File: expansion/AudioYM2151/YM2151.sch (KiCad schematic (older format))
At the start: 14 parts

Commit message: More work on YM2151
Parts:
- added C? (x5): 100nF, symbol Device:C
- added RN?: R_Network05, Resistor_THT:R_Array_SIP6, symbol Device:R_Network05
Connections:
- net GNDA is gone; now on net GND: C?.1, C?.1, C?.2, C?.2, U?.11 (V-), U?.16 (AGND), U?.8 (AGND)
- net +5V: now also C?.1, C?.1, C?.1, C?.1, C?.1, RN?.1 (common)
- net GND: now also C?.2, C?.2, C?.2, C?.2, C?.2
- net ~IRQ: now also RN?.2 (R1)
- net at U?.19 (SH2), U?.5 (SAM2): now also RN?.5 (R4)
- net at U?.20 (SH1), U?.6 (SAM1): now also RN?.4 (R3)
- net at U?.21 (SO), U?.4 (SD): now also RN?.3 (R2)
- net at U?.2 (CLK1), U?.23 (1): now also RN?.6 (R5)
- net D0 renamed D8
- net D1 renamed D9
- net D2 renamed D10
- net D3 renamed D11
- net D4 renamed D12
- net D5 renamed D13
- net D6 renamed D14
- net D7 renamed D15
- net SPI_YMCLK renamed CS_YMCLK
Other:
- moved on the sheet: C?, R?, U?, U?A, U?B, U?C, U?D, U?E

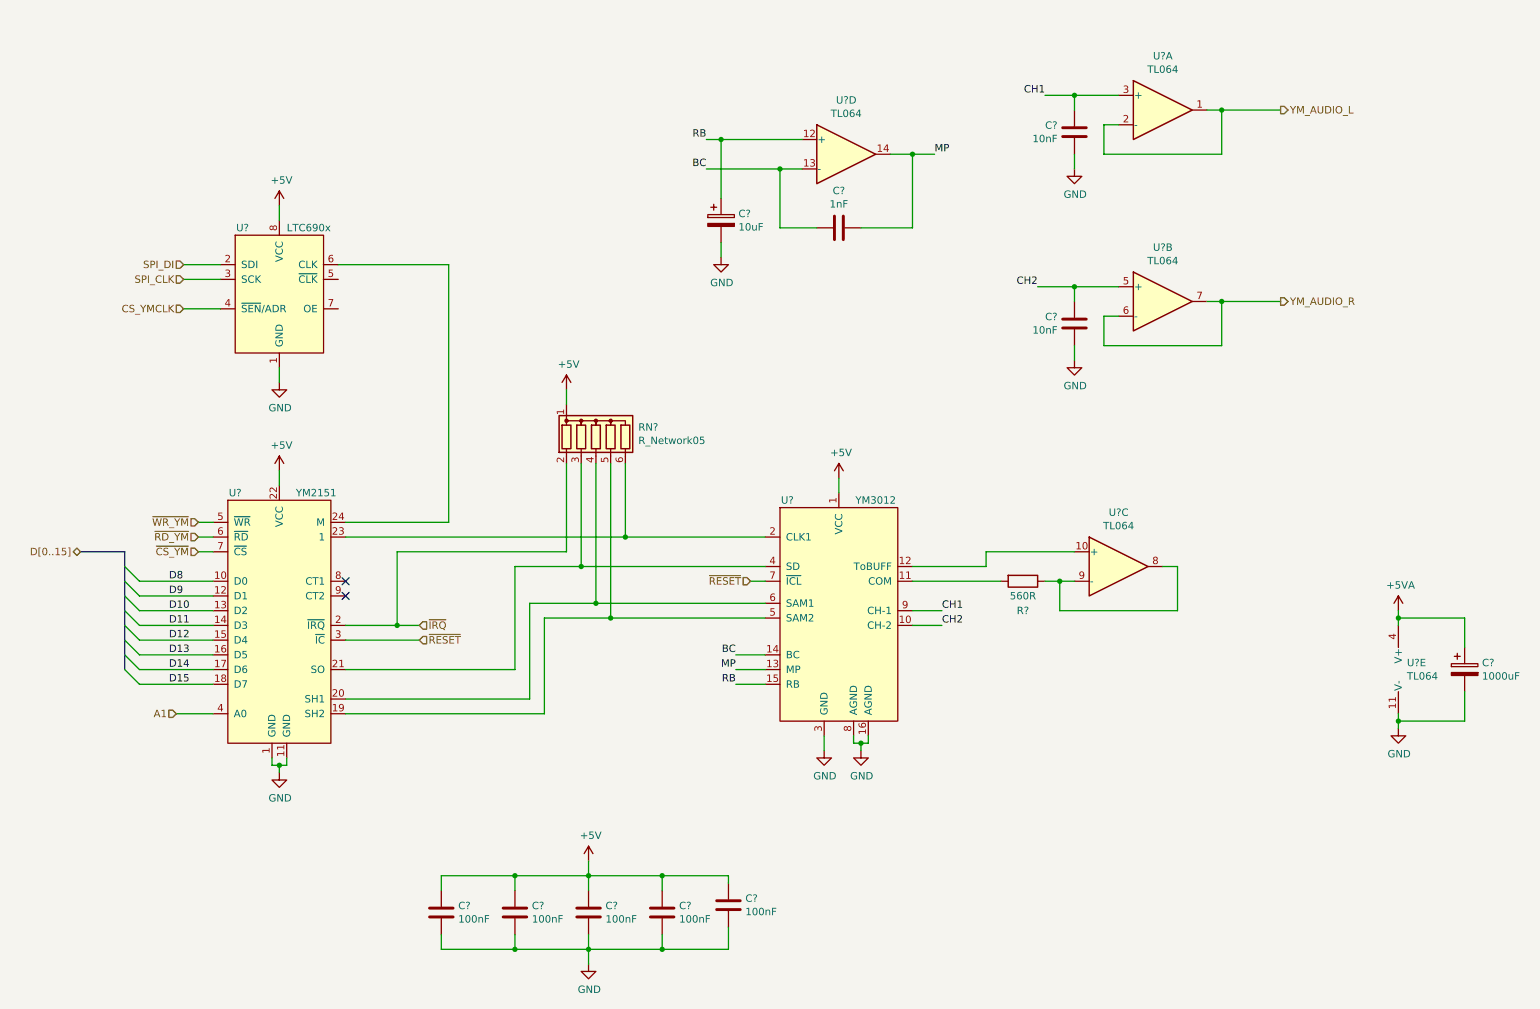
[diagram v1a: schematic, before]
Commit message: Started YM2151 board layout
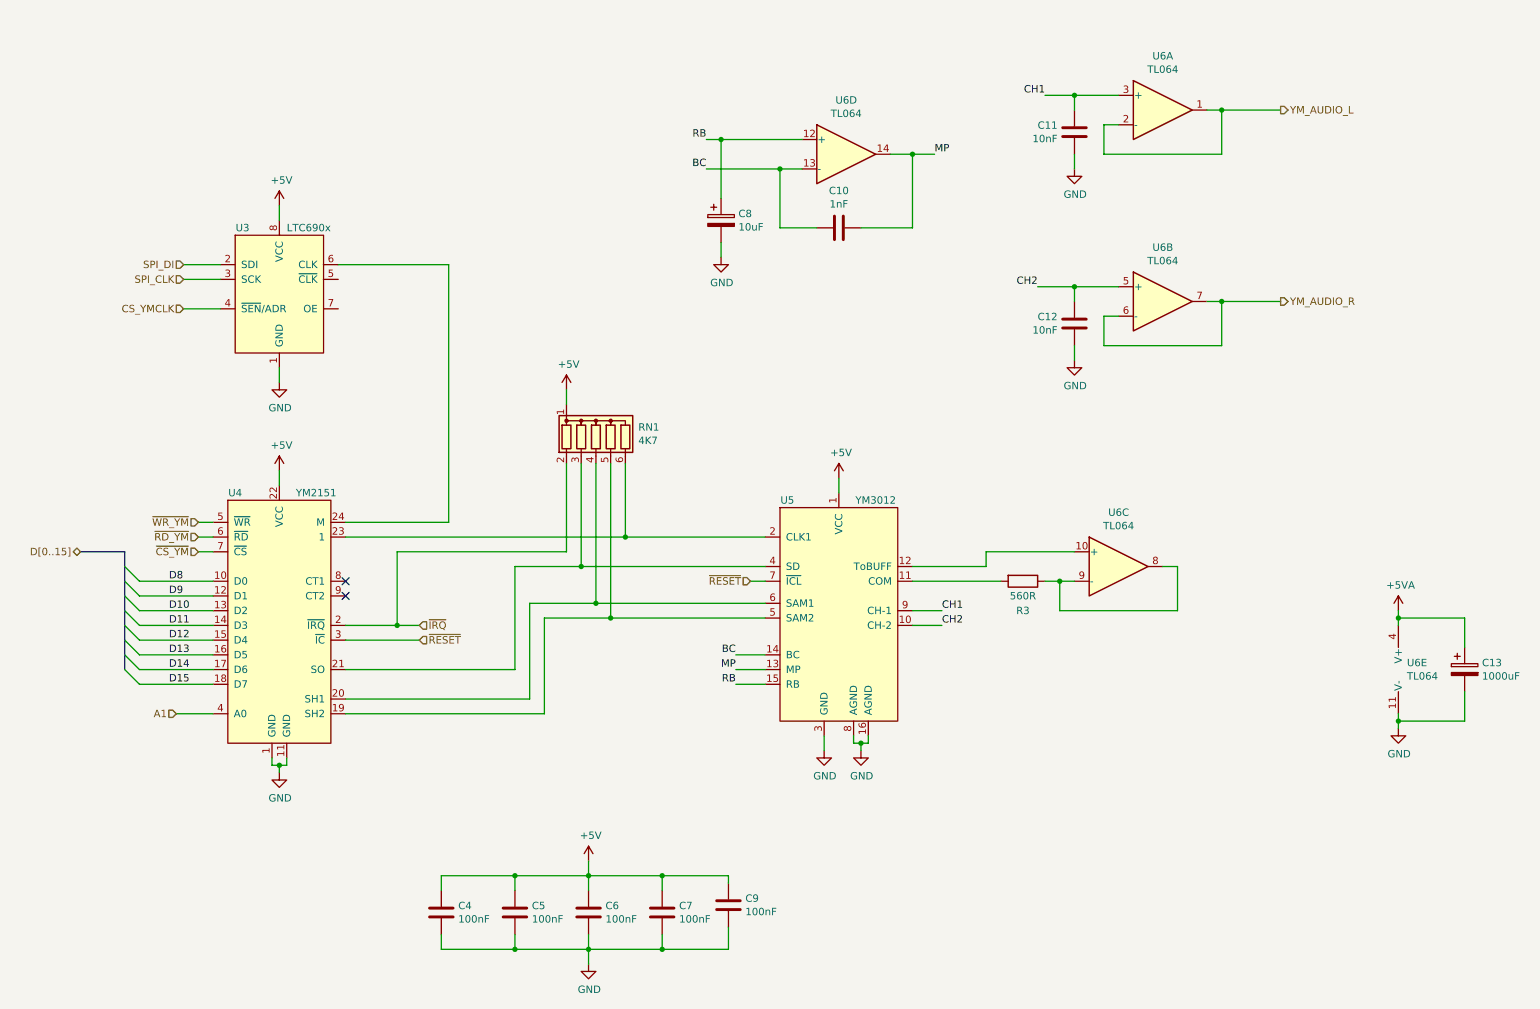
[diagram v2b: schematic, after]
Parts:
- C10, C11, C12, C4, C5, C6, C7, C9: renamed from C?; footprint (none) -> Capacitor_THT:C_Disc_D5.0mm_W2.5mm_P2.50mm
- C13: renamed from C?; footprint (none) -> Capacitor_THT:CP_Radial_D8.0mm_P5.00mm
- C8: renamed from C?; footprint (none) -> Capacitor_THT:CP_Radial_D5.0mm_P2.50mm
- R3: renamed from R?; footprint (none) -> Resistor_THT:R_Axial_DIN0207_L6.3mm_D2.5mm_P10.16mm_Horizontal
- RN1: renamed from RN?; value R_Network05 -> 4K7
- U3: renamed from U?; footprint (none) -> Package_SO:MSOP-8_3x3mm_P0.65mm
- U5: renamed from U?; footprint (none) -> Package_DIP:DIP-16_W7.62mm_Socket
- U6: renamed from U?; footprint (none) -> Package_DIP:DIP-14_W7.62mm_Socket
- gave numbers to parts that had none: 1

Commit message: YM2151 Initial board placement done
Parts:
- added C46: 10nF, Capacitor_THT:C_Disc_D5.0mm_W2.5mm_P2.50mm, symbol Device:C
- C13: value 1000uF -> 220uF; footprint Capacitor_THT:CP_Radial_D8.0mm_P5.00mm -> Capacitor_THT:CP_Radial_D5.0mm_P2.50mm
- U4: footprint Package_DIP:DIP-24_W15.24mm -> Package_DIP:DIP-24_W15.24mm_Socket
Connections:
- net +5VA is gone; now on net +5V: C13.1, U6.4 (V+)
- net +5V: now also U3.7 (OE), C46.1
- net GND: now also C46.2
- no-connect marks 2 -> 3
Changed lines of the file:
@@
 F 0 "U4" H 2250 6000 50  0000 C CNN
 F 1 "YM2151" H 2800 6000 50  0000 C CNN
-F 2 "Package_DIP:DIP-24_W15.24mm" H 2550 5100 50  0001 C CNN
+F 2 "Package_DIP:DIP-24_W15.24mm_Socket" H 2550 5100 50  0001 C CNN
 F 3 "" H 2550 5100 50  0001 C CNN
 	1    2550 5100
@@
 P 10600 5400
 F 0 "C13" H 10718 5446 50  0000 L CNN
-F 1 "1000uF" H 10718 5355 50  0000 L CNN
-F 2 "Capacitor_THT:CP_Radial_D8.0mm_P5.00mm" H 10638 5250 50  0001 C CNN
+F 1 "220uF" H 10718 5355 50  0000 L CNN
+F 2 "Capacitor_THT:CP_Radial_D5.0mm_P2.50mm" H 10638 5250 50  0001 C CNN
 F 3 "~" H 10600 5400 50  0001 C CNN
 	1    10600 5400
@@
 Wire Wire Line
 	5850 5500 5650 5500
-$Comp
-L power:+5VA #PWR0116
-U 1 1 60C5CEB4
-P 10150 5000
-F 0 "#PWR0116" H 10150 4850 50  0001 C CNN
-F 1 "+5VA" H 10165 5173 50  0000 C CNN
-F 2 "" H 10150 5000 50  0001 C CNN
-F 3 "" H 10150 5000 50  0001 C CNN
-	1    10150 5000
-	1    0    0    -1
-$EndComp
 Wire Wire Line
 	10150 5000 10150 5050
@@
 	5600 6800 5150 6800
 Connection ~ 5150 6800
+NoConn ~ 2950 2750
+$Comp
+L Device:C C46
+U 1 1 61537371
+P 3100 3200
+F 0 "C46" H 3215 3246 50  0000 L CNN
+F 1 "10nF" H 3215 3155 50  0000 L CNN
+F 2 "Capacitor_THT:C_Disc_D5.0mm_W2.5mm_P2.50mm" H 3138 3050 50  0001 C CNN
+F 3 "~" H 3100 3200 50  0001 C CNN
+	1    3100 3200
+	1    0    0    -1
+$EndComp
+$Comp
+L power:GND #PWR0172
+U 1 1 6153751F
+P 3100 3450
+F 0 "#PWR0172" H 3100 3200 50  0001 C CNN
+F 1 "GND" H 3105 3277 50  0000 C CNN
+F 2 "" H 3100 3450 50  0001 C CNN
+F 3 "" H 3100 3450 50  0001 C CNN
+	1    3100 3450
+	1    0    0    -1
+$EndComp
+$Comp
+L power:+5V #PWR0173
+U 1 1 61537D3F
+P 3100 2250
+F 0 "#PWR0173" H 3100 2100 50  0001 C CNN
+F 1 "+5V" H 3115 2423 50  0000 C CNN
+F 2 "" H 3100 2250 50  0001 C CNN
+F 3 "" H 3100 2250 50  0001 C CNN
+	1    3100 2250
+	1    0    0    -1
+$EndComp
+Wire Wire Line
+	3100 2250 3100 2950
+Wire Wire Line
+	3100 3450 3100 3350
+Wire Wire Line
+	2950 2950 3100 2950
 Wire Bus Line
 	1500 4600 1500 5400
+Connection ~ 3100 2950
+Wire Wire Line
+	3100 2950 3100 3050
+$Comp
+L power:+5V #PWR0116
+U 1 1 6154C49A
+P 10150 5000
+F 0 "#PWR0116" H 10150 4850 50  0001 C CNN
+F 1 "+5V" H 10165 5173 50  0000 C CNN
+F 2 "" H 10150 5000 50  0001 C CNN
+F 3 "" H 10150 5000 50  0001 C CNN
+	1    10150 5000
+	1    0    0    -1
+$EndComp
 $EndSCHEMATC

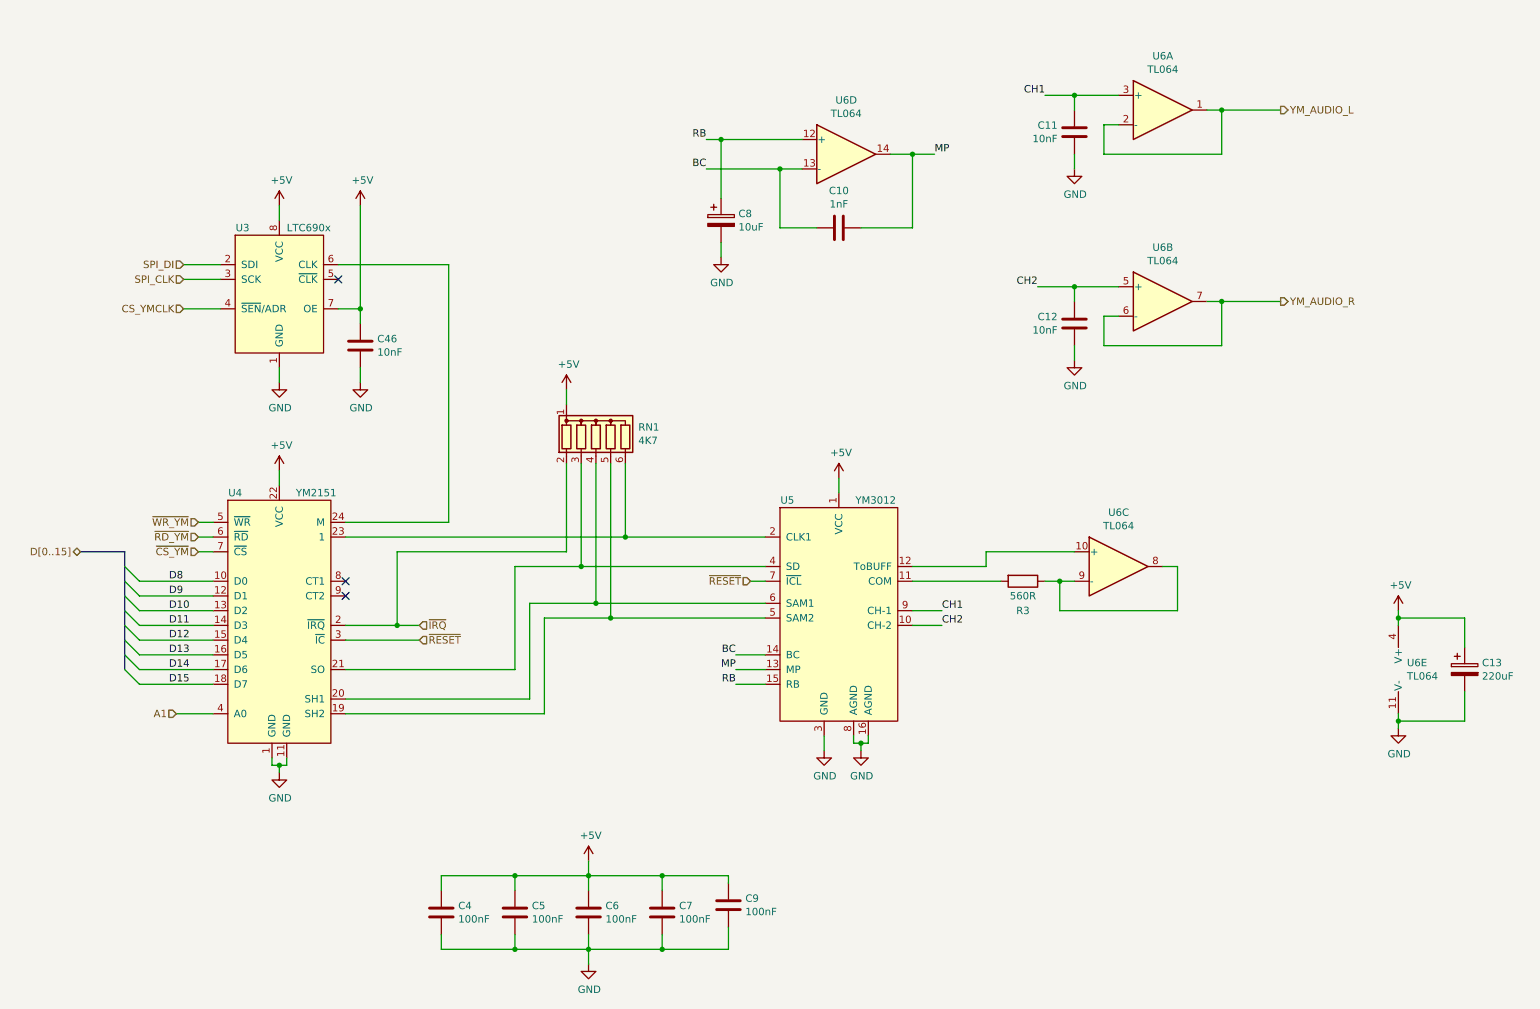
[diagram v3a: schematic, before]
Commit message: Removed MSM ADPCM chip from YM2151 board
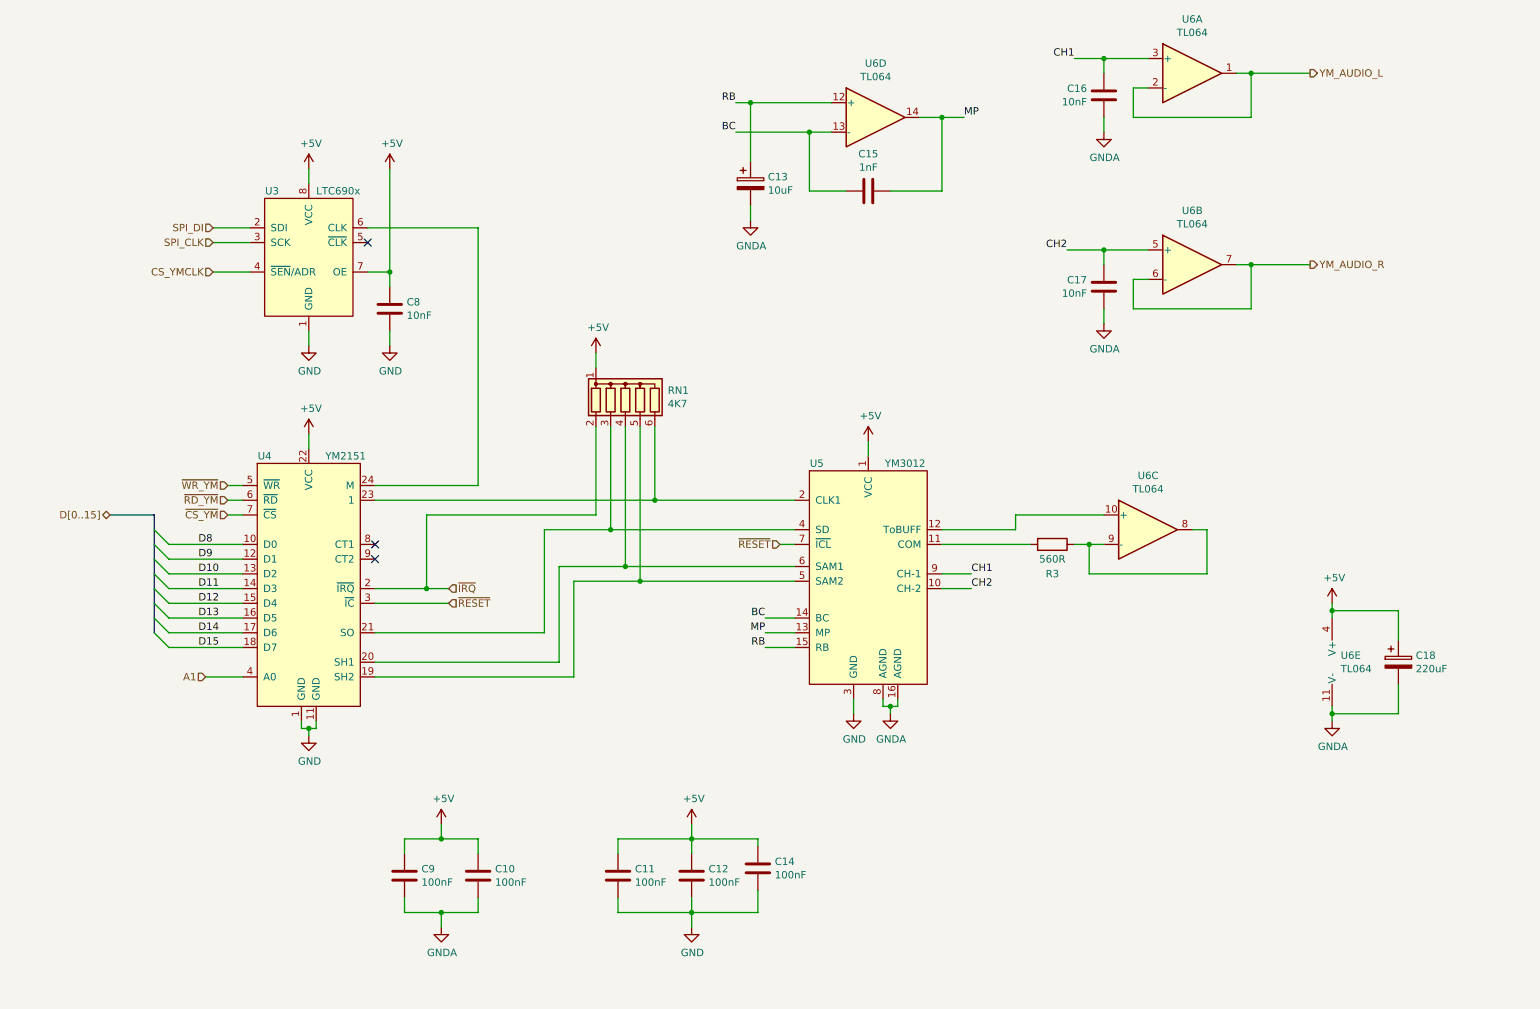
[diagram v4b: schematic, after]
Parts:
- renumbered C5 to C10, C6 to C11, C7 to C12, C8 to C13, C9 to C14, C10 to C15, C11 to C16, C12 to C17, C13 to C18, C46 to C8, C4 to C9
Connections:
- net GND: no longer C10.2, C13.2, C16.1, C17.1, C18.2, C9.2, U5.16 (AGND), U5.8 (AGND), U6.11 (V-)
- new net GNDA: C10.2, C13.2, C16.1, C17.1, C18.2, C9.2, U5.16 (AGND), U5.8 (AGND), U6.11 (V-)
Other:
- moved on the sheet: C10, C11, C12, C13, C14, C15, C16, C17, C18, C8, C9, R3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
